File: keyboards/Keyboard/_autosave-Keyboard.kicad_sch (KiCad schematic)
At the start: 92 parts

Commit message: added backupfiles and contents
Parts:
- added U1, U2: RP2040_Zero, ScottoKeebs_MCU:RP2040_Zero, symbol ScottoKeebs:MCU_RP2040_Zero
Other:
- moved on the sheet: D1, D10, D11, D12, D13, D14, D15, D16, D17, D18, D19, D2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

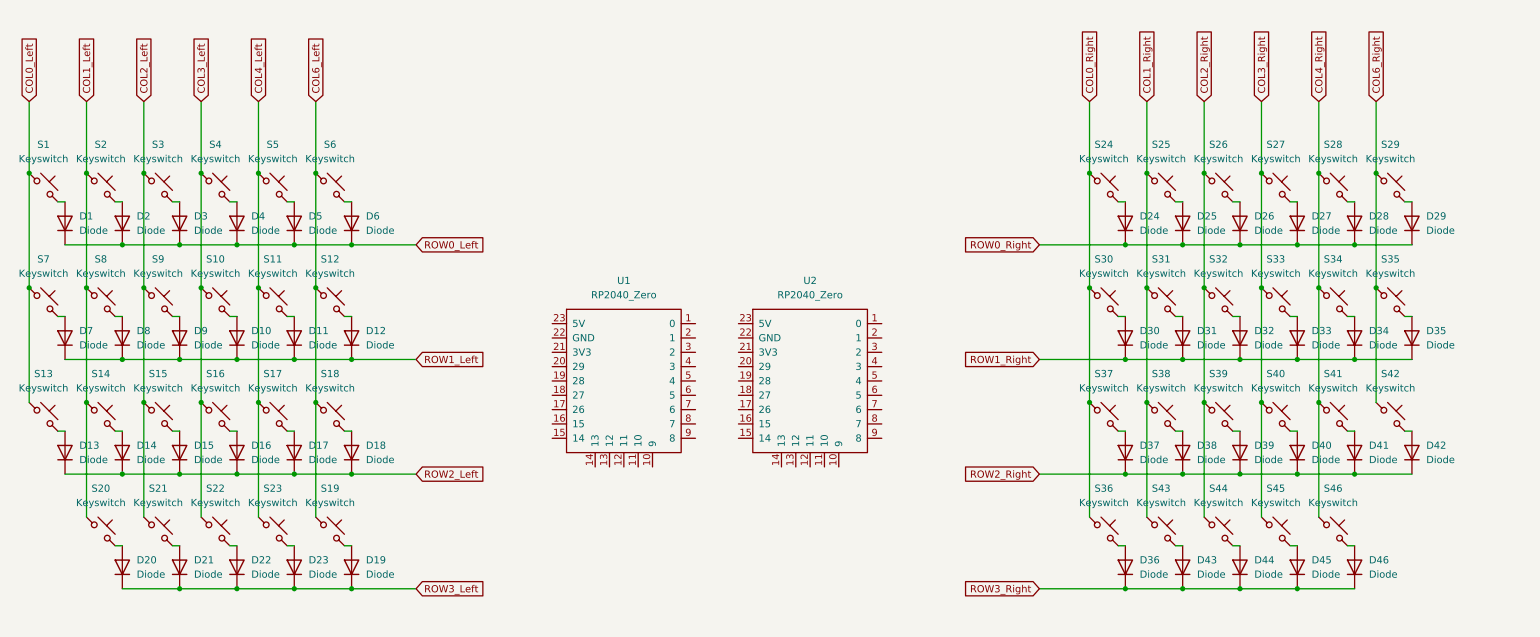
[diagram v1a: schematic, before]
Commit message: add TRRS Connection
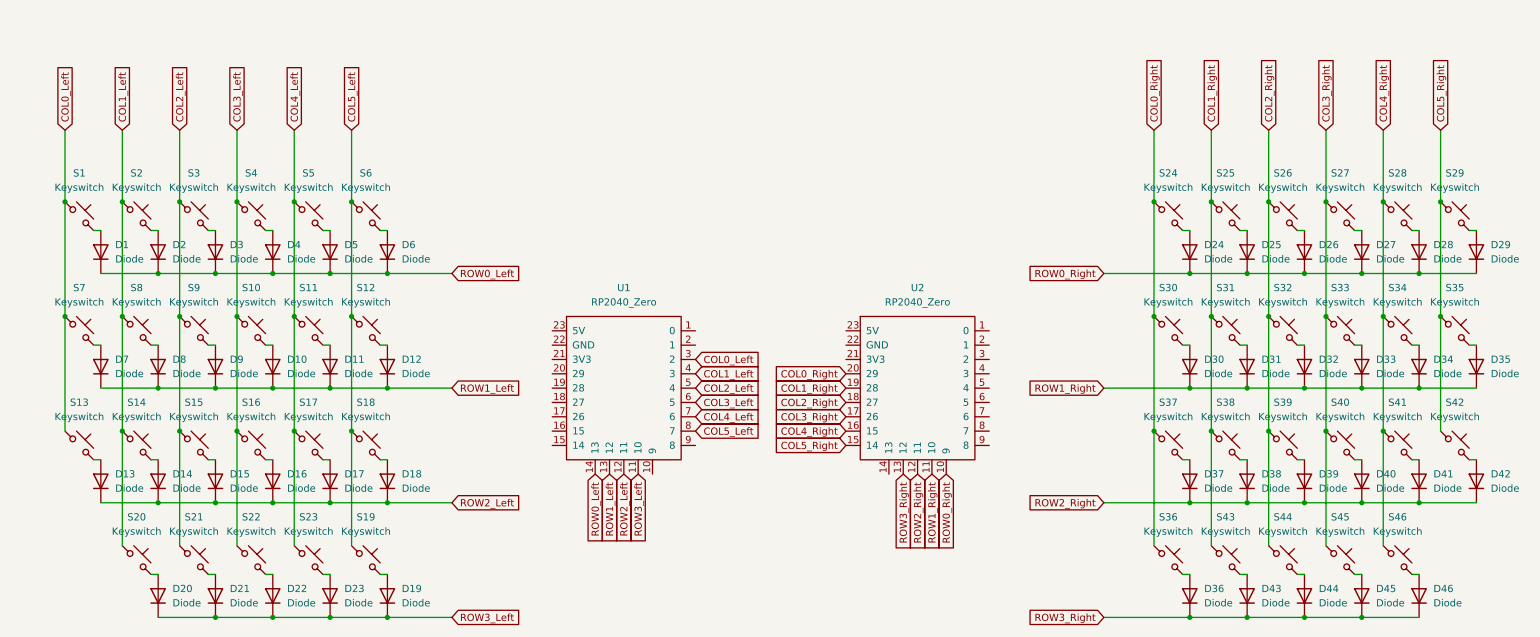
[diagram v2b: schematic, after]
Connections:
- net COL6_Left is gone; now on net COL5_Left: S12.1, S18.1, S19.1, S6.1
- net COL6_Right is gone; now on net COL5_Right: S29.1, S35.1, S42.1
- net COL0_Left: now also U1.3 (2)
- net COL0_Right: now also U2.20 (29)
- net COL1_Left: now also U1.4 (3)
- net COL1_Right: now also U2.19 (28)
- net COL2_Left: now also U1.5 (4)
- net COL2_Right: now also U2.18 (27)
- net COL3_Left: now also U1.6 (5)
- net COL3_Right: now also U2.17 (26)
- net COL4_Left: now also U1.7 (6)
- net COL4_Right: now also U2.16 (15)
- net ROW0_Left: now also U1.14 (13)
- net ROW0_Right: now also U2.10 (9)
- net ROW1_Left: now also U1.13 (12)
- net ROW1_Right: now also U2.11 (10)
- net ROW2_Left: now also U1.12 (11)
- net ROW2_Right: now also U2.12 (11)
- net ROW3_Left: now also U1.11 (10)
- net ROW3_Right: now also U2.13 (12)
- net COL5_Right: now reaches U2.15 (14)
- net COL5_Left: now reaches U1.8 (7)
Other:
- moved on the sheet: D1, D10, D11, D12, D13, D14, D15, D16, D17, D18, D19, D2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
